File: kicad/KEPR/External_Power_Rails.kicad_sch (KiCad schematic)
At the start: 14 parts, among them J1 PINHD_1x20_Male, J12 PINHD_1x20_Male, J16 PINHD_1x10_Male, J17 PINHD_1x20_Male, J19 PINHD_1x20_Male, J22 Barrel_Jack, J23 PINHD_1x10_Male, J24 PINHD_2x2_Male, J26 PINHD_2x3_Male, J30 PINHD_2x2_Male, U4 AMS1117-1.8

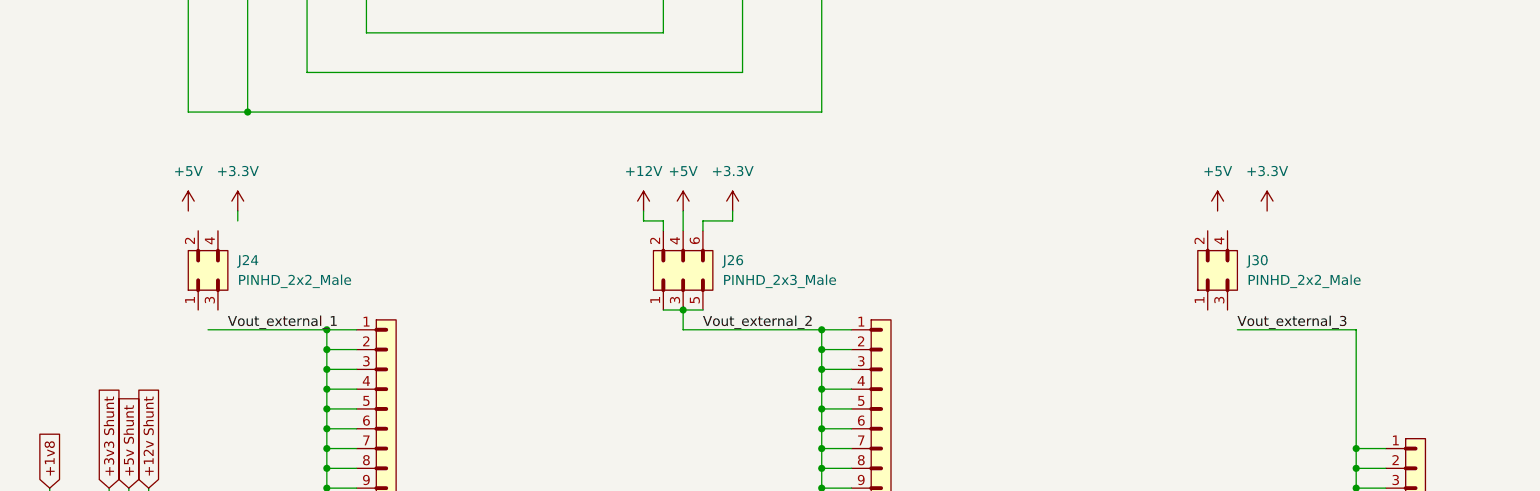
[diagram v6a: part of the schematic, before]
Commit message: Ajustando trilhas
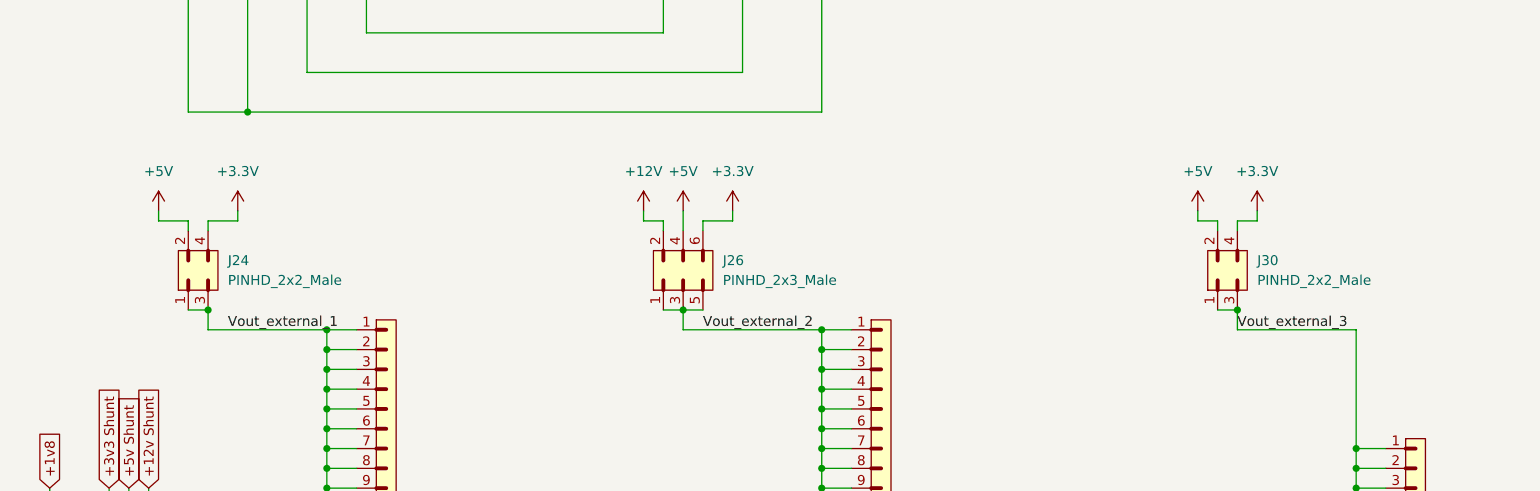
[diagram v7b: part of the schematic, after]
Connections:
- net +3.3V: now also J24.4, J30.4
- net +5V: now also J24.2, J30.2
- net Vout_external_1: now also J24.1, J24.3
- net Vout_external_3: now also J30.1, J30.3
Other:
- moved on the sheet: J24, J30
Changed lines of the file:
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@@
 	)
 	(junction
+		(at 246.38 81.28)
+		(diameter 0)
+		(color 0 0 0 0)
+	)
+	(junction
 		(at 130.81 167.64)
 		(diameter 0)
@@
 	)
 	(junction
+		(at 114.3 81.28)
+		(diameter 0)
+		(color 0 0 0 0)
+	)
+	(junction
 		(at 193.04 93.98)
 		(diameter 0)
@@
 	(wire
 		(pts
+			(xy 111.76 81.28) (xy 114.3 81.28)
+		)
+		(stroke
+			(width 0)
+			(type default)
+		)
+	)
+	(wire
+		(pts
 			(xy 130.81 172.72) (xy 130.81 175.26)
 		)
@@
 	(wire
 		(pts
+			(xy 246.38 69.85) (xy 248.92 69.85)
+		)
+		(stroke
+			(width 0)
+			(type default)
+		)
+	)
+	(wire
+		(pts
 			(xy 194.31 180.34) (xy 194.31 182.88)
 		)
@@
 	(wire
 		(pts
+			(xy 241.3 69.85) (xy 243.84 69.85)
+		)
+		(stroke
+			(width 0)
+			(type default)
+		)
+	)
+	(wire
+		(pts
 			(xy 114.3 83.82) (xy 129.54 83.82)
 		)
@@
 	(wire
 		(pts
+			(xy 111.76 69.85) (xy 111.76 71.12)
+		)
+		(stroke
+			(width 0)
+			(type default)
+		)
+	)
+	(wire
+		(pts
 			(xy 93.98 119.38) (xy 93.98 104.14)
 		)
@@
 	(wire
 		(pts
-			(xy 118.11 68.58) (xy 118.11 69.85)
+			(xy 118.11 69.85) (xy 118.11 68.58)
 		)
 		(stroke
@@
 	(wire
 		(pts
+			(xy 107.95 68.58) (xy 107.95 69.85)
+		)
+		(stroke
+			(width 0)
+			(type default)
+		)
+	)
+	(wire
+		(pts
+			(xy 246.38 69.85) (xy 246.38 71.12)
+		)
+		(stroke
+			(width 0)
+			(type default)
+		)
+	)
+	(wire
+		(pts
 			(xy 194.31 182.88) (xy 196.85 182.88)
 		)
@@
 	(wire
 		(pts
+			(xy 243.84 69.85) (xy 243.84 71.12)
+		)
+		(stroke
+			(width 0)
+			(type default)
+		)
+	)
+	(wire
+		(pts
 			(xy 194.31 185.42) (xy 194.31 187.96)
 		)
@@
 	(wire
 		(pts
+			(xy 241.3 69.85) (xy 241.3 68.58)
+		)
+		(stroke
+			(width 0)
+			(type default)
+		)
+	)
+	(wire
+		(pts
 			(xy 193.04 124.46) (xy 193.04 121.92)
 		)
@@
 	(wire
 		(pts
+			(xy 107.95 69.85) (xy 111.76 69.85)
+		)
+		(stroke
+			(width 0)
+			(type default)
+		)
+	)
+	(wire
+		(pts
 			(xy 194.31 170.18) (xy 194.31 172.72)
 		)
@@
 	(wire
 		(pts
+			(xy 243.84 81.28) (xy 246.38 81.28)
+		)
+		(stroke
+			(width 0)
+			(type default)
+		)
+	)
+	(wire
+		(pts
 			(xy 193.04 104.14) (xy 193.04 101.6)
 		)
@@
 	(wire
 		(pts
+			(xy 114.3 69.85) (xy 114.3 71.12)
+		)
+		(stroke
+			(width 0)
+			(type default)
+		)
+	)
+	(wire
+		(pts
 			(xy 261.62 116.84) (xy 261.62 114.3)
 		)
@@
 	(wire
 		(pts
+			(xy 114.3 69.85) (xy 118.11 69.85)
+		)
+		(stroke
+			(width 0)
+			(type default)
+		)
+	)
+	(wire
+		(pts
 			(xy 127 35.56) (xy 127 50.8)
 		)
@@
 	(wire
 		(pts
+			(xy 246.38 81.28) (xy 246.38 83.82)
+		)
+		(stroke
+			(width 0)
+			(type default)
+		)
+	)
+	(wire
+		(pts
 			(xy 170.18 68.58) (xy 170.18 69.85)
 		)
@@
 	(wire
 		(pts
+			(xy 248.92 69.85) (xy 248.92 68.58)
+		)
+		(stroke
+			(width 0)
+			(type default)
+		)
+	)
+	(wire
+		(pts
 			(xy 262.89 190.5) (xy 262.89 193.04)
 		)
@@
 	(wire
 		(pts
+			(xy 114.3 81.28) (xy 114.3 83.82)
+		)
+		(stroke
+			(width 0)
+			(type default)
+		)
+	)
+	(wire
+		(pts
 			(xy 130.81 160.02) (xy 130.81 162.56)
 		)
@@
 	(symbol
 		(lib_id "PCM_SL_Pin_Headers:PINHD_2x2_Male")
-		(at 114.3 76.2 90)
+		(at 113.03 76.2 90)
 		(unit 1)
 		(exclude_from_sim yes)
@@
 		(fields_autoplaced yes)
 		(property "Reference" "J24"
-			(at 118.11 74.9299 90)
+			(at 116.84 74.9299 90)
 			(effects
 				(font
@@
 		)
 		(property "Value" "PINHD_2x2_Male"
-			(at 118.11 77.4699 90)
+			(at 116.84 77.4699 90)
 			(effects
 				(font
@@
 		)
 		(property "Footprint" "Connector_PinHeader_2.54mm:PinHeader_2x02_P2.54mm_Vertical"
-			(at 118.11 76.2 0)
+			(at 116.84 76.2 0)
 			(effects
 				(font
@@
 		)
 		(property "Datasheet" ""
-			(at 106.68 77.47 0)
+			(at 105.41 77.47 0)
 			(effects
 				(font
@@
 		)
 		(property "Description" "Pin Header male with pin space 2.54mm. Pin Count -4"
-			(at 114.3 76.2 0)
+			(at 113.03 76.2 0)
 			(effects
 				(font
@@
 	(symbol
 		(lib_id "power:+5V")
-		(at 111.76 68.58 0)
+		(at 107.95 68.58 0)
 		(unit 1)
 		(exclude_from_sim no)
@@
 		(fields_autoplaced yes)
 		(property "Reference" "#PWR07"
-			(at 111.76 72.39 0)
+			(at 107.95 72.39 0)
 			(effects
 				(font
@@
 		)
 		(property "Value" "+5V"
-			(at 111.76 63.5 0)
+			(at 107.95 63.5 0)
 			(effects
 				(font
@@
 		)
 		(property "Footprint" ""
-			(at 111.76 68.58 0)
+			(at 107.95 68.58 0)
 			(effects
 				(font
@@
 		)
 		(property "Datasheet" ""
-			(at 111.76 68.58 0)
+			(at 107.95 68.58 0)
 			(effects
 				(font
@@
 		)
 		(property "Description" "Power symbol creates a global label with name \"+5V\""
-			(at 111.76 68.58 0)
+			(at 107.95 68.58 0)
 			(effects
 				(font
@@
 	(symbol
 		(lib_id "PCM_SL_Pin_Headers:PINHD_2x2_Male")
-		(at 243.84 76.2 90)
+		(at 245.11 76.2 90)
 		(unit 1)
 		(exclude_from_sim no)
@@
 		(on_board yes)
 		(dnp no)
-		(fields_autoplaced yes)
 		(property "Reference" "J30"
-			(at 247.65 74.9299 90)
+			(at 248.92 74.9299 90)
 			(effects
 				(font
@@
 		)
 		(property "Value" "PINHD_2x2_Male"
-			(at 247.65 77.4699 90)
+			(at 248.92 77.4699 90)
 			(effects
 				(font
@@
 		)
 		(property "Footprint" "Connector_PinHeader_2.54mm:PinHeader_2x02_P2.54mm_Vertical"
-			(at 247.65 76.2 0)
+			(at 248.92 76.2 0)
 			(effects
 				(font
@@
 		)
 		(property "Datasheet" ""
-			(at 236.22 77.47 0)
+			(at 237.49 77.47 0)
 			(effects
 				(font
@@
 		)
 		(property "Description" "Pin Header male with pin space 2.54mm. Pin Count -4"
-			(at 243.84 76.2 0)
+			(at 245.11 76.2 0)
 			(effects
 				(font
@@
 	(symbol
 		(lib_id "power:+5V")
-		(at 243.84 68.58 0)
+		(at 241.3 68.58 0)
 		(unit 1)
 		(exclude_from_sim no)
@@
 		(fields_autoplaced yes)
 		(property "Reference" "#PWR021"
-			(at 243.84 72.39 0)
+			(at 241.3 72.39 0)
 			(effects
 				(font
@@
 		)
 		(property "Value" "+5V"
-			(at 243.84 63.5 0)
+			(at 241.3 63.5 0)
 			(effects
 				(font
@@
 		)
 		(property "Footprint" ""
-			(at 243.84 68.58 0)
+			(at 241.3 68.58 0)
 			(effects
 				(font
@@
 		)
 		(property "Datasheet" ""
-			(at 243.84 68.58 0)
+			(at 241.3 68.58 0)
 			(effects
 				(font
@@
 		)
 		(property "Description" "Power symbol creates a global label with name \"+5V\""
-			(at 243.84 68.58 0)
+			(at 241.3 68.58 0)
 			(effects
 				(font
@@
 	(symbol
 		(lib_id "power:+3.3V")
-		(at 250.19 68.58 0)
+		(at 248.92 68.58 0)
 		(unit 1)
 		(exclude_from_sim no)
@@
 		(fields_autoplaced yes)
 		(property "Reference" "#PWR022"
-			(at 250.19 72.39 0)
+			(at 248.92 72.39 0)
 			(effects
 				(font
@@
 		)
 		(property "Value" "+3.3V"
-			(at 250.19 63.5 0)
+			(at 248.92 63.5 0)
 			(effects
 				(font
@@
 		)
 		(property "Footprint" ""
-			(at 250.19 68.58 0)
+			(at 248.92 68.58 0)
 			(effects
 				(font
@@
 		)
 		(property "Datasheet" ""
-			(at 250.19 68.58 0)
+			(at 248.92 68.58 0)
 			(effects
 				(font
@@
 		)
 		(property "Description" "Power symbol creates a global label with name \"+3.3V\""
-			(at 250.19 68.58 0)
+			(at 248.92 68.58 0)
 			(effects
 				(font

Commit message: mais ajustes de trilha.
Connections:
- net GND: no longer PS1.5 (NC), PS2.5 (NC), PS3.5 (NC)
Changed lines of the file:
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@@
-	)
-	(junction
-		(at 101.6 215.9)
-		(diameter 0)
-		(color 0 0 0 0)
-	)
-	(junction
-		(at 99.06 152.4)
-		(diameter 0)
-		(color 0 0 0 0)
 	)
 	(junction
@@
 	)
 	(junction
-		(at 101.6 182.88)
-		(diameter 0)
-		(color 0 0 0 0)
-	)
-	(junction
 		(at 194.31 172.72)
 		(diameter 0)
@@
 	(wire
 		(pts
-			(xy 99.06 147.32) (xy 99.06 152.4)
-		)
-		(stroke
-			(width 0)
-			(type default)
-		)
-	)
-	(wire
-		(pts
 			(xy 261.62 114.3) (xy 265.43 114.3)
 		)
@@
 	(wire
 		(pts
-			(xy 101.6 180.34) (xy 101.6 182.88)
-		)
-		(stroke
-			(width 0)
-			(type default)
-		)
-	)
-	(wire
-		(pts
-			(xy 101.6 210.82) (xy 101.6 215.9)
-		)
-		(stroke
-			(width 0)
-			(type default)
-		)
-	)
-	(wire
-		(pts
 			(xy 193.04 121.92) (xy 196.85 121.92)
 		)
@@
 	(wire
 		(pts
-			(xy 99.06 177.8) (xy 99.06 180.34)
-		)
-		(stroke
-			(width 0)
-			(type default)
-		)
-	)
-	(wire
-		(pts
 			(xy 63.5 152.4) (xy 40.64 152.4)
 		)
@@
 	(wire
 		(pts
-			(xy 99.06 180.34) (xy 101.6 180.34)
-		)
-		(stroke
-			(width 0)
-			(type default)
-		)
-	)
-	(wire
-		(pts
 			(xy 181.61 69.85) (xy 177.8 69.85)
 		)
@@
 	(wire
 		(pts
-			(xy 99.06 182.88) (xy 101.6 182.88)
+			(xy 99.06 182.88) (xy 109.22 182.88)
 		)
 		(stroke
@@
 		(pts
 			(xy 134.62 35.56) (xy 134.62 45.72)
-		)
-		(stroke
-			(width 0)
-			(type default)
-		)
-	)
-	(wire
-		(pts
-			(xy 101.6 182.88) (xy 109.22 182.88)
 		)
 		(stroke
@@
 			)
 		)
+	)
+	(rule_area
+		(polyline
+			(pts
+				(xy 104.14 22.86) (xy 201.93 22.86) (xy 201.93 58.42) (xy 105.41 58.42) (xy 104.14 57.15)
+			)
+			(stroke
+				(width 0)
+				(type dash)
+			)
+			(fill
+				(type none)
+			)
+		)
+	)
+	(rule_area
+		(polyline
+			(pts
+				(xy 97.79 87.63) (xy 110.49 87.63) (xy 110.49 106.68) (xy 97.79 106.68)
+			)
+			(stroke
+				(width 0)
+				(type dash)
+			)
+			(fill
+				(type none)
+			)
+		)
+	)
+	(netclass_flag ""
+		(length 2.54)
+		(shape round)
+		(at 102.87 87.63 0)
+		(fields_autoplaced yes)
+		(effects
+			(font
+				(size 1.27 1.27)
+			)
+			(justify left bottom)
+		)
+		(property "Netclass" "Shunt"
+			(at 103.5685 85.09 0)
+			(effects
+				(font
+					(size 1.27 1.27)
+				)
+				(justify left)
+			)
+		)
+		(property "Component Class" ""
+			(at -102.87 13.97 0)
+			(effects
+				(font
+					(size 1.27 1.27)
+					(italic yes)
+				)
+			)
+		)
+	)
+	(netclass_flag ""
+		(length 2.54)
+		(shape round)
+		(at 128.27 22.86 0)
+		(fields_autoplaced yes)
+		(effects
+			(font
+				(size 1.27 1.27)
+			)
+			(justify left bottom)
+		)
+		(property "Netclass" "Main Power Rail"
+			(at 128.9685 20.32 0)
+			(effects
+				(font
+					(size 1.27 1.27)
+				)
+				(justify left)
+			)
+		)
+		(property "Component Class" ""
+			(at -20.32 3.81 0)
+			(effects
+				(font
+					(size 1.27 1.27)
+					(italic yes)
+				)
+			)
+		)
